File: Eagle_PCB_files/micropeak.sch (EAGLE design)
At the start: 15 parts, among them U1 ATTINY85-20MUR, U2 MS5611-01BA03

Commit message: have holes and outline positioned correctly - floorplanning done pretty much
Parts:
- removed H1, H2, H3, H4: MOUNT-PAD-ROUND2.8, holes:MOUNT-PAD-ROUND2.8
- removed LED1: (no value), led:LEDP-LCC-2
- added U$3: LED, LED_LYT68B-T2V1-26-Z:LED
- added U$4, U$5, U$6, U$7: (no value), LED_LYT68B-T2V1-26-Z:MOUNT_HOLE
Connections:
- net +3V3: now also U$4.MOUNT, U$5.MOUNT, U$6.MOUNT, U$7.MOUNT; no longer H1.MOUNT, H2.MOUNT, H3.MOUNT, H4.MOUNT
- net GND: now also U$3.C; no longer LED1.C
- net N$4: now also U$3.A; no longer LED1.A
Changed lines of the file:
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@@
 <part name="+3V4" library="supply1" library_urn="urn:adsk.eagle:library:371" deviceset="+3V3" device=""/>
 <part name="+3V5" library="supply1" library_urn="urn:adsk.eagle:library:371" deviceset="+3V3" device=""/>
-<part name="LED1" library="led" library_urn="urn:adsk.eagle:library:259" deviceset="LED" device="P-LCC-2" package3d_urn="urn:adsk.eagle:package:15817/1"/>
-<part name="H4" library="holes" library_urn="urn:adsk.eagle:library:237" deviceset="MOUNT-PAD-ROUND" device="2.8" package3d_urn="urn:adsk.eagle:package:14281/1"/>
-<part name="H1" library="holes" library_urn="urn:adsk.eagle:library:237" deviceset="MOUNT-PAD-ROUND" device="2.8" package3d_urn="urn:adsk.eagle:package:14281/1"/>
-<part name="H2" library="holes" library_urn="urn:adsk.eagle:library:237" deviceset="MOUNT-PAD-ROUND" device="2.8" package3d_urn="urn:adsk.eagle:package:14281/1"/>
-<part name="H3" library="holes" library_urn="urn:adsk.eagle:library:237" deviceset="MOUNT-PAD-ROUND" device="2.8" package3d_urn="urn:adsk.eagle:package:14281/1"/>
+<part name="U$3" library="LED_LYT68B-T2V1-26-Z" deviceset="LED" device=""/>
+<part name="U$4" library="LED_LYT68B-T2V1-26-Z" deviceset="MOUNT_HOLE" device=""/>
+<part name="U$5" library="LED_LYT68B-T2V1-26-Z" deviceset="MOUNT_HOLE" device=""/>
+<part name="U$6" library="LED_LYT68B-T2V1-26-Z" deviceset="MOUNT_HOLE" device=""/>
+<part name="U$7" library="LED_LYT68B-T2V1-26-Z" deviceset="MOUNT_HOLE" device=""/>
 </parts>
 <sheets>
@@
 <attribute name="VALUE" x="38.1" y="52.07" size="1.778" layer="96" rot="R90"/>
 </instance>
-<instance part="LED1" gate="G$1" x="194.056" y="135.89" smashed="yes" rot="R90">
+<instance part="U$3" gate="G$1" x="194.056" y="135.89" smashed="yes" rot="R90">
 <attribute name="NAME" x="198.628" y="139.446" size="1.778" layer="95" rot="R180"/>
 <attribute name="VALUE" x="198.628" y="141.605" size="1.778" layer="96" rot="R180"/>
 </instance>
-<instance part="H4" gate="G$1" x="48.26" y="45.72" smashed="yes">
+<instance part="U$4" gate="G$1" x="48.26" y="45.72" smashed="yes">
 <attribute name="NAME" x="51.054" y="46.3042" size="1.778" layer="95"/>
 <attribute name="VALUE" x="51.054" y="43.2562" size="1.778" layer="96"/>
 </instance>
-<instance part="H1" gate="G$1" x="48.26" y="38.1" smashed="yes">
+<instance part="U$5" gate="G$1" x="48.26" y="38.1" smashed="yes">
 <attribute name="NAME" x="51.054" y="38.6842" size="1.778" layer="95"/>
 <attribute name="VALUE" x="51.054" y="35.6362" size="1.778" layer="96"/>
 </instance>
-<instance part="H2" gate="G$1" x="48.26" y="30.48" smashed="yes">
+<instance part="U$6" gate="G$1" x="48.26" y="30.48" smashed="yes">
 <attribute name="NAME" x="51.054" y="31.0642" size="1.778" layer="95"/>
 <attribute name="VALUE" x="51.054" y="28.0162" size="1.778" layer="96"/>
 </instance>
-<instance part="H3" gate="G$1" x="48.26" y="22.86" smashed="yes">
+<instance part="U$7" gate="G$1" x="48.26" y="22.86" smashed="yes">
 <attribute name="NAME" x="51.054" y="23.4442" size="1.778" layer="95"/>
 <attribute name="VALUE" x="51.054" y="20.3962" size="1.778" layer="96"/>
@@
 <wire x1="199.39" y1="135.89" x2="200.66" y2="135.89" width="0.1524" layer="91"/>
 <pinref part="U1" gate="G$1" pin="EXP"/>
-<wire x1="200.66" y1="134.62" x2="200.66" y2="128.27" width="0.1524" layer="91"/>
+<wire x1="200.66" y1="135.89" x2="200.66" y2="128.27" width="0.1524" layer="91"/>
 <wire x1="200.66" y1="128.27" x2="200.66" y2="125.73" width="0.1524" layer="91"/>
 <wire x1="200.66" y1="125.73" x2="200.66" y2="114.3" width="0.1524" layer="91"/>
@@
 <wire x1="200.66" y1="143.51" x2="200.66" y2="135.89" width="0.1524" layer="91"/>
 <junction x="200.66" y="135.89"/>
-<pinref part="LED1" gate="G$1" pin="C"/>
 <wire x1="199.136" y1="135.89" x2="200.66" y2="135.89" width="0.1524" layer="91"/>
-<wire x1="200.66" y1="135.89" x2="200.66" y2="134.62" width="0.1524" layer="91"/>
+<pinref part="U$3" gate="G$1" pin="C"/>
 </segment>
 <segment>
@@
 <wire x1="40.64" y1="22.86" x2="40.64" y2="30.48" width="0.1524" layer="91"/>
 <junction x="40.64" y="30.48"/>
-<pinref part="H4" gate="G$1" pin="MOUNT"/>
-<pinref part="H1" gate="G$1" pin="MOUNT"/>
-<pinref part="H2" gate="G$1" pin="MOUNT"/>
-<pinref part="H3" gate="G$1" pin="MOUNT"/>
+<pinref part="U$4" gate="G$1" pin="MOUNT"/>
+<pinref part="U$5" gate="G$1" pin="MOUNT"/>
+<pinref part="U$6" gate="G$1" pin="MOUNT"/>
+<pinref part="U$7" gate="G$1" pin="MOUNT"/>
 </segment>
 </net>
@@
 <net name="N$4" class="0">
 <segment>
-<pinref part="LED1" gate="G$1" pin="A"/>
 <pinref part="R1" gate="G$1" pin="2"/>
 <wire x1="191.516" y1="135.89" x2="189.23" y2="135.89" width="0.1524" layer="91"/>
-</segment>
-</net>
+<pinref part="U$3" gate="G$1" pin="A"/>
+</segment>
+</net>

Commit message: routing done
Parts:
- removed C2: (no value), rcl:C-EUC0603
- removed R3: (no value), rcl:R-EU_R0603
- added C3: (no value), rcl:C-EUC0402
- added R4: (no value), rcl:R-EU_R0402
- C1: device rcl:C-EUC0603 -> rcl:C-EUC0402
- R1, R2: device rcl:R-EU_R0603 -> rcl:R-EU_R0402
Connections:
- new net N$11: U$1.GND@3
- new net N$12: U$1.GND@4
- net +3V3: now also C3.1, R4.2; no longer C2.1, R2.2
- net GND: now also C3.2; no longer C2.2, U$1.GND@3, U$1.GND@4
- net MOSI: now also R1.1; no longer R3.1
- net N$2: now also R4.1; no longer R2.1
- net N$3: now also R2.2; no longer R1.1
- net N$4: now also R2.1; no longer R1.2
- net N$5: now also R1.2; no longer R3.2
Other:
- moved on the sheet: C1, R1, R2

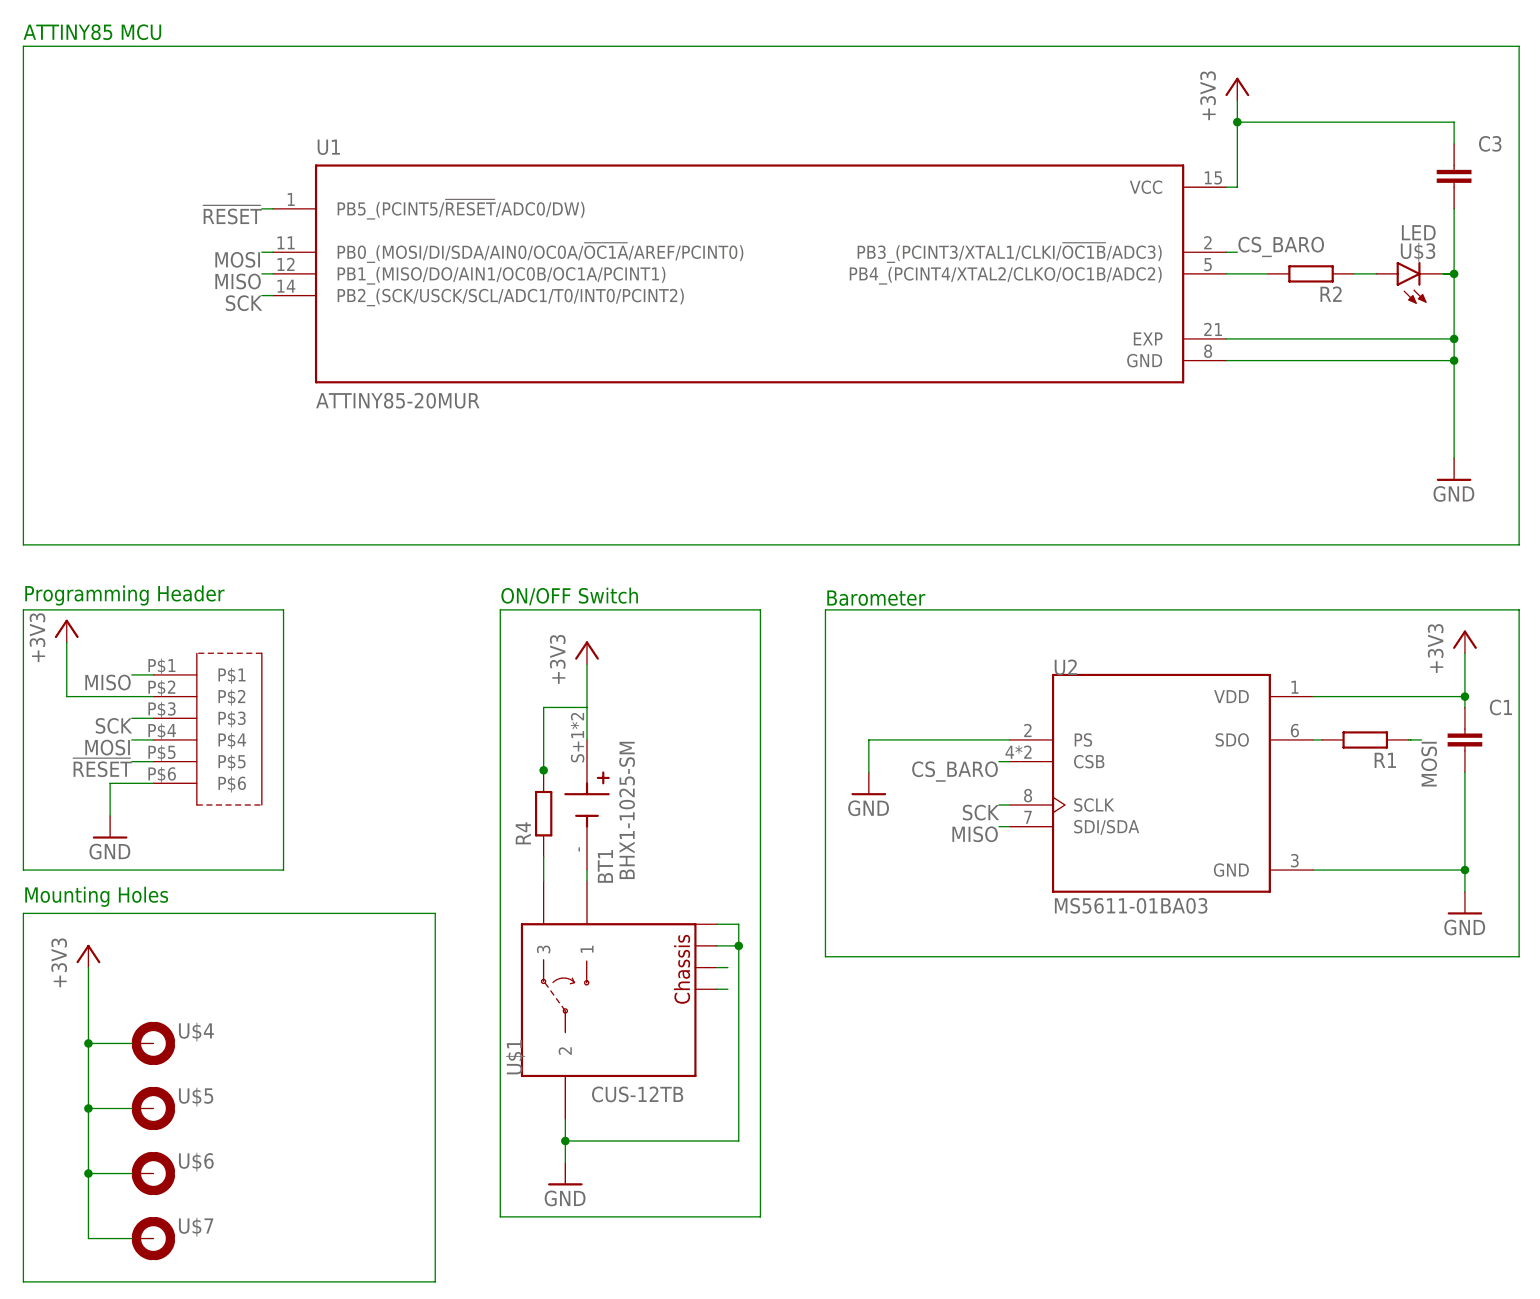
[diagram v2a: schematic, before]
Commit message: added resistor values
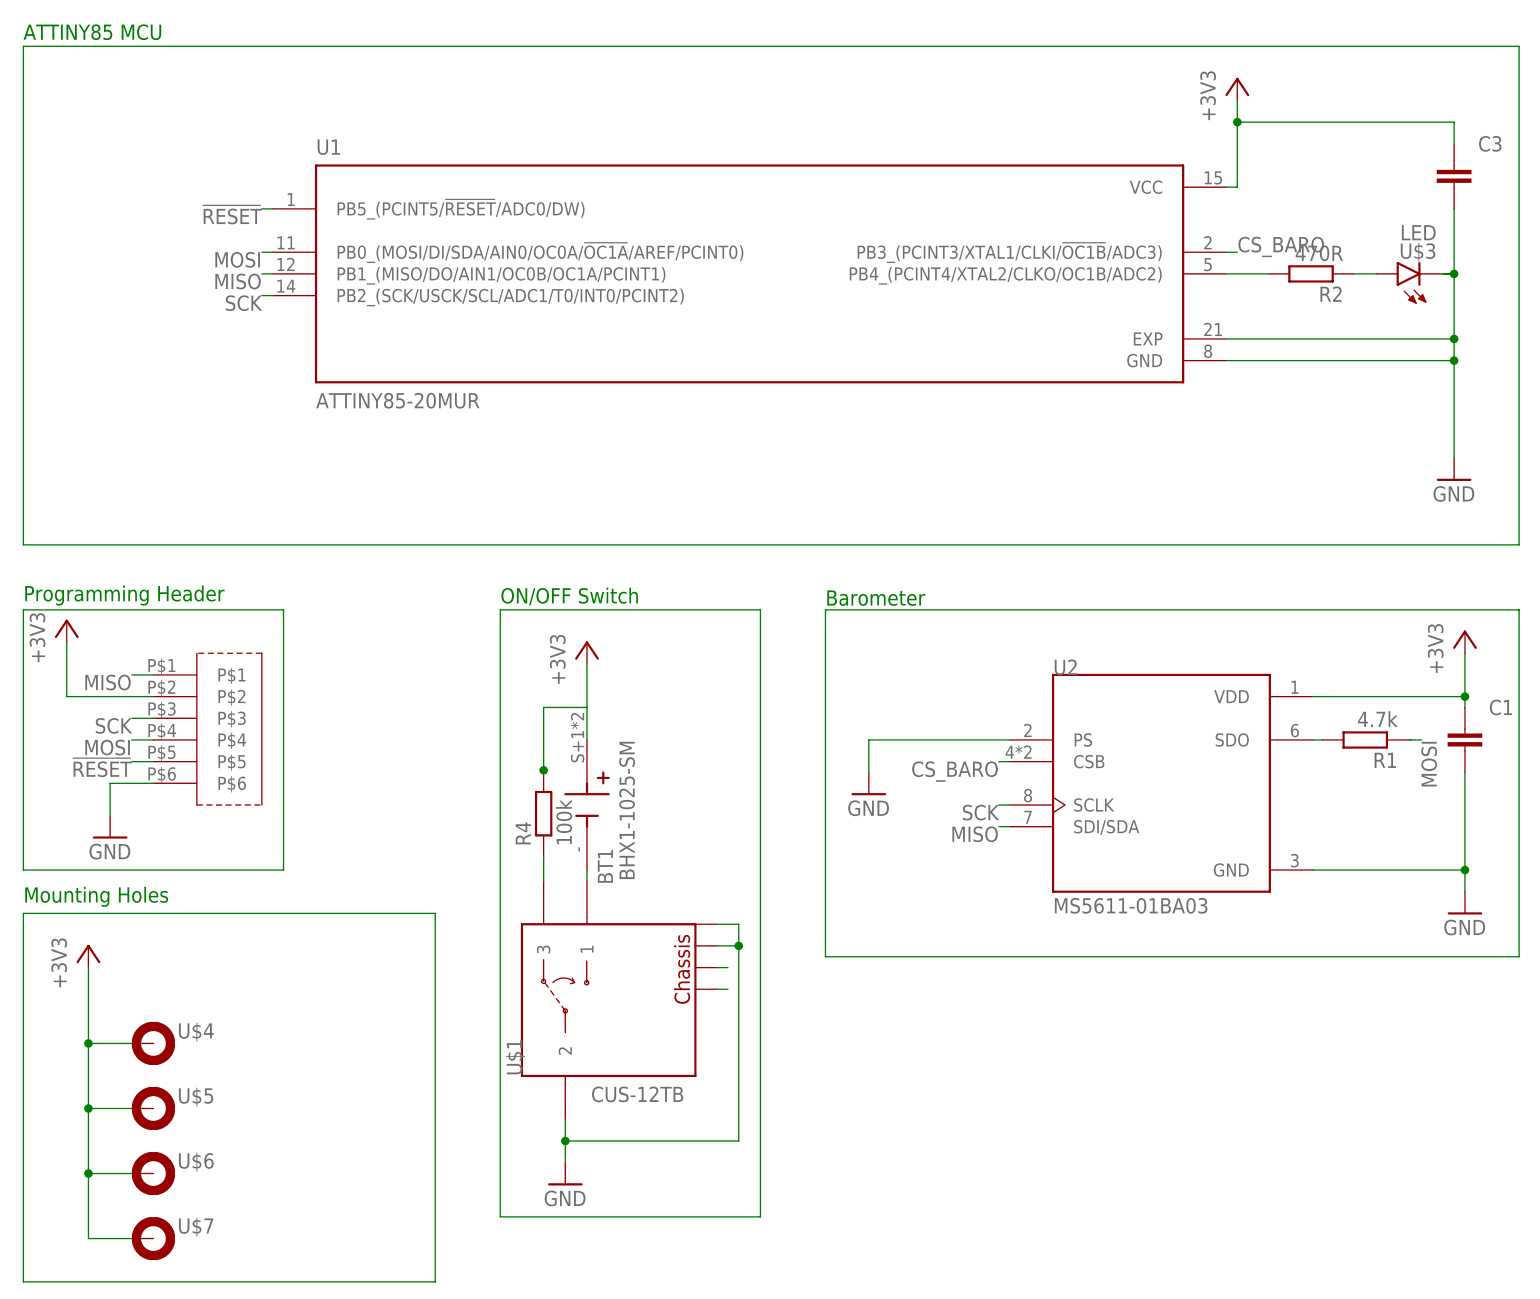
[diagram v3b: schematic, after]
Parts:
- R1: value (none) -> 4.7k
- R2: value (none) -> 470R
- R4: value (none) -> 100k
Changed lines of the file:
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@@
 <part name="U$6" library="LED_LYT68B-T2V1-26-Z" deviceset="MOUNT_HOLE" device=""/>
 <part name="U$7" library="LED_LYT68B-T2V1-26-Z" deviceset="MOUNT_HOLE" device=""/>
-<part name="R4" library="rcl" library_urn="urn:adsk.eagle:library:334" deviceset="R-EU_" device="R0402" package3d_urn="urn:adsk.eagle:package:23547/3"/>
-<part name="R1" library="rcl" library_urn="urn:adsk.eagle:library:334" deviceset="R-EU_" device="R0402" package3d_urn="urn:adsk.eagle:package:23547/3"/>
-<part name="R2" library="rcl" library_urn="urn:adsk.eagle:library:334" deviceset="R-EU_" device="R0402" package3d_urn="urn:adsk.eagle:package:23547/3"/>
+<part name="R4" library="rcl" library_urn="urn:adsk.eagle:library:334" deviceset="R-EU_" device="R0402" package3d_urn="urn:adsk.eagle:package:23547/3" value="100k"/>
+<part name="R1" library="rcl" library_urn="urn:adsk.eagle:library:334" deviceset="R-EU_" device="R0402" package3d_urn="urn:adsk.eagle:package:23547/3" value="4.7k"/>
+<part name="R2" library="rcl" library_urn="urn:adsk.eagle:library:334" deviceset="R-EU_" device="R0402" package3d_urn="urn:adsk.eagle:package:23547/3" value="470R"/>
 <part name="C3" library="rcl" library_urn="urn:adsk.eagle:library:334" deviceset="C-EU" device="C0402" package3d_urn="urn:adsk.eagle:package:23626/2"/>
 <part name="C1" library="rcl" library_urn="urn:adsk.eagle:library:334" deviceset="C-EU" device="C0402" package3d_urn="urn:adsk.eagle:package:23626/2"/>
